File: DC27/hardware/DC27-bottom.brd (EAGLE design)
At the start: 102.4 x 117.6 mm, 97 parts, among them IC2 LDL112D33R, IC3 FT2232HL-REEL, IC4 93LC46BT-I_OT, J1 PAIRING, J2 JTAG, J3 Battery, J4 Program Port, U2 ESP-WROOM-32, Y1 ABM7-12.000MHZ-D2Y-T

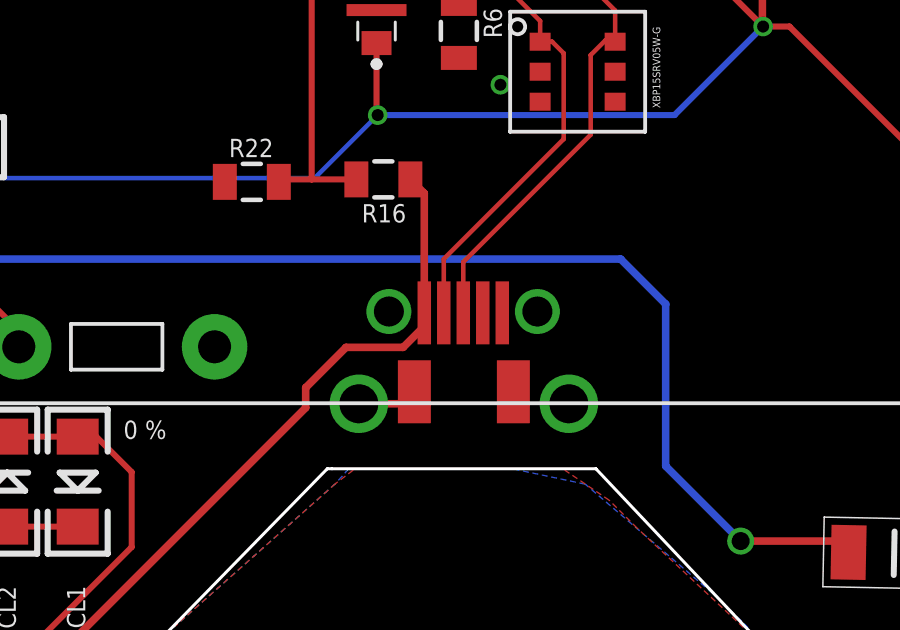
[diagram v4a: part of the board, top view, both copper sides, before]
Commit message: moved usb .15mm closer to edge per first pcb ask
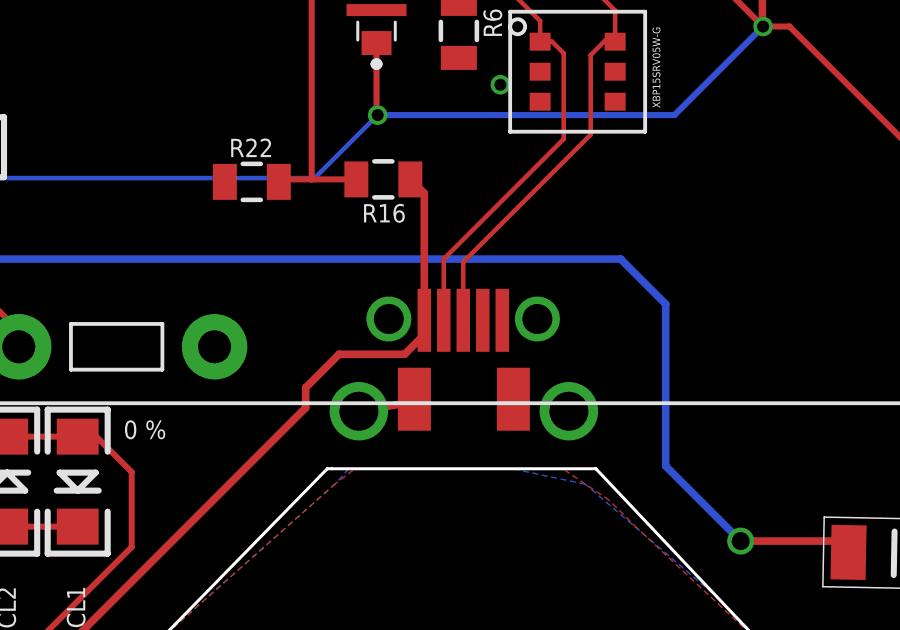
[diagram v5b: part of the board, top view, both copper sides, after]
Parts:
- moved U$3 0.25 mm to (51.2, 27.8)
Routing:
- net VCC5V: track 42.3 -> 43.0 mm
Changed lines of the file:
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@@
 <attribute name="RS_PRICE/STOCK" value="" x="68.550228125" y="45.380659375" size="1.778" layer="27" display="off"/>
 </element>
-<element name="U$3" library="connector" package="DX4R005JJ2" value="DX4R005JJ2DX4R005JJ2" x="51.207428125" y="28.016259375" smashed="yes" rot="R270"/>
+<element name="U$3" library="connector" package="DX4R005JJ2" value="DX4R005JJ2DX4R005JJ2" x="51.207428125" y="27.766259375" smashed="yes" rot="R270"/>
 <element name="RESETTABLE_FUSE" library="passives" package="FUSC3216X55N" value="0ZCJ0050FF2G" x="65.550228125" y="19.282659375" smashed="yes" rot="R358.9">
 <attribute name="3D_PACKAGE" value="" x="47.390459375" y="57.890790625" size="1.778" layer="27" rot="R358.9" display="off"/>
@@
 <via x="37.934228125" y="58.989059375" extent="1-16" drill="0.4"/>
 <via x="48.534228125" y="73.689059375" extent="1-16" drill="0.4"/>
-<wire x1="47.707428125" y1="24.266259375" x2="49.157428125" y2="24.266259375" width="0.254" layer="1"/>
-<wire x1="49.157428125" y1="24.266259375" x2="49.557428125" y2="24.666259375" width="0.254" layer="1"/>
+<wire x1="47.707428125" y1="24.016259375" x2="49.157428125" y2="24.266259375" width="0.254" layer="1"/>
+<wire x1="49.157428125" y1="24.266259375" x2="49.557428125" y2="24.416259375" width="0.254" layer="1"/>
 <via x="40.934228125" y="62.389059375" extent="1-16" drill="0.4"/>
 <via x="54.634228125" y="74.289059375" extent="1-16" drill="0.4"/>
@@
 <wire x1="35.0368625" y1="13.235059375" x2="27.667828125" y2="13.235059375" width="0.254" layer="1"/>
 <wire x1="27.667828125" y1="13.235059375" x2="27.267828125" y2="12.835059375" width="0.254" layer="1"/>
-<wire x1="49.887428125" y1="27.296259375" x2="49.887978125" y2="27.295709375" width="0.254" layer="1"/>
-<wire x1="49.887978125" y1="27.295709375" x2="49.887978125" y2="26.850096875" width="0.254" layer="1"/>
-<wire x1="47.277315625" y1="26.146059375" x2="45.934228125" y2="24.802971875" width="0.254" layer="1"/>
-<wire x1="49.887978125" y1="26.850096875" x2="49.183940625" y2="26.146059375" width="0.254" layer="1"/>
-<wire x1="49.183940625" y1="26.146059375" x2="47.277315625" y2="26.146059375" width="0.254" layer="1"/>
+<wire x1="49.887428125" y1="27.046259375" x2="49.887978125" y2="27.295709375" width="0.254" layer="1"/>
+<wire x1="49.887978125" y1="27.295709375" x2="49.887978125" y2="26.570096875" width="0.254" layer="1"/>
+<wire x1="47.047315625" y1="25.916059375" x2="45.934228125" y2="24.802971875" width="0.254" layer="1"/>
+<wire x1="49.887978125" y1="26.570096875" x2="49.233940625" y2="25.916059375" width="0.254" layer="1"/>
+<wire x1="49.233940625" y1="25.916059375" x2="47.047315625" y2="25.916059375" width="0.254" layer="1"/>
 <wire x1="27.267828125" y1="12.835059375" x2="24.917828125" y2="15.185059375" width="0.254" layer="1"/>
 <wire x1="24.917828125" y1="15.185059375" x2="23.233428125" y2="15.185059375" width="0.254" layer="1"/>
 <wire x1="35.0368625" y1="13.235059375" x2="45.934228125" y2="24.132425" width="0.254" layer="1"/>
 <wire x1="45.934228125" y1="24.132425" x2="45.934228125" y2="24.802971875" width="0.254" layer="1"/>
-<wire x1="49.887428125" y1="27.296259375" x2="49.887428125" y2="31.281459375" width="0.254" layer="1"/>
+<wire x1="49.887428125" y1="27.046259375" x2="49.887428125" y2="31.281459375" width="0.254" layer="1"/>
 <wire x1="49.887428125" y1="31.281459375" x2="49.423428125" y2="31.745459375" width="0.254" layer="1"/>
 <wire x1="23.233428125" y1="15.185059375" x2="23.233428125" y2="15.970759375" width="0.254" layer="1"/>
@@
 <contactref element="IC3" pad="8"/>
 <contactref element="U$2" pad="P6"/>
-<wire x1="51.187428125" y1="27.296259375" x2="51.187428125" y2="28.989059375" width="0.1524" layer="1"/>
+<wire x1="51.187428125" y1="27.046259375" x2="51.187428125" y2="28.989059375" width="0.1524" layer="1"/>
 <wire x1="52.334228125" y1="39.489059375" x2="53.584228125" y2="38.239059375" width="0.1524" layer="1"/>
 <wire x1="52.334228125" y1="39.489059375" x2="52.334228125" y2="56.847859375" width="0.1524" layer="1"/>
@@
 <wire x1="53.749828125" y1="36.334259375" x2="54.149828125" y2="36.334259375" width="0.1524" layer="1"/>
 <wire x1="54.534228125" y1="33.089059375" x2="54.534228125" y2="35.949859375" width="0.1524" layer="1"/>
-<wire x1="50.537428125" y1="27.296259375" x2="50.537428125" y2="29.092259375" width="0.1524" layer="1"/>
+<wire x1="50.537428125" y1="27.046259375" x2="50.537428125" y2="29.092259375" width="0.1524" layer="1"/>
 <wire x1="50.537428125" y1="29.092259375" x2="54.534228125" y2="33.089059375" width="0.1524" layer="1"/>
 </signal>

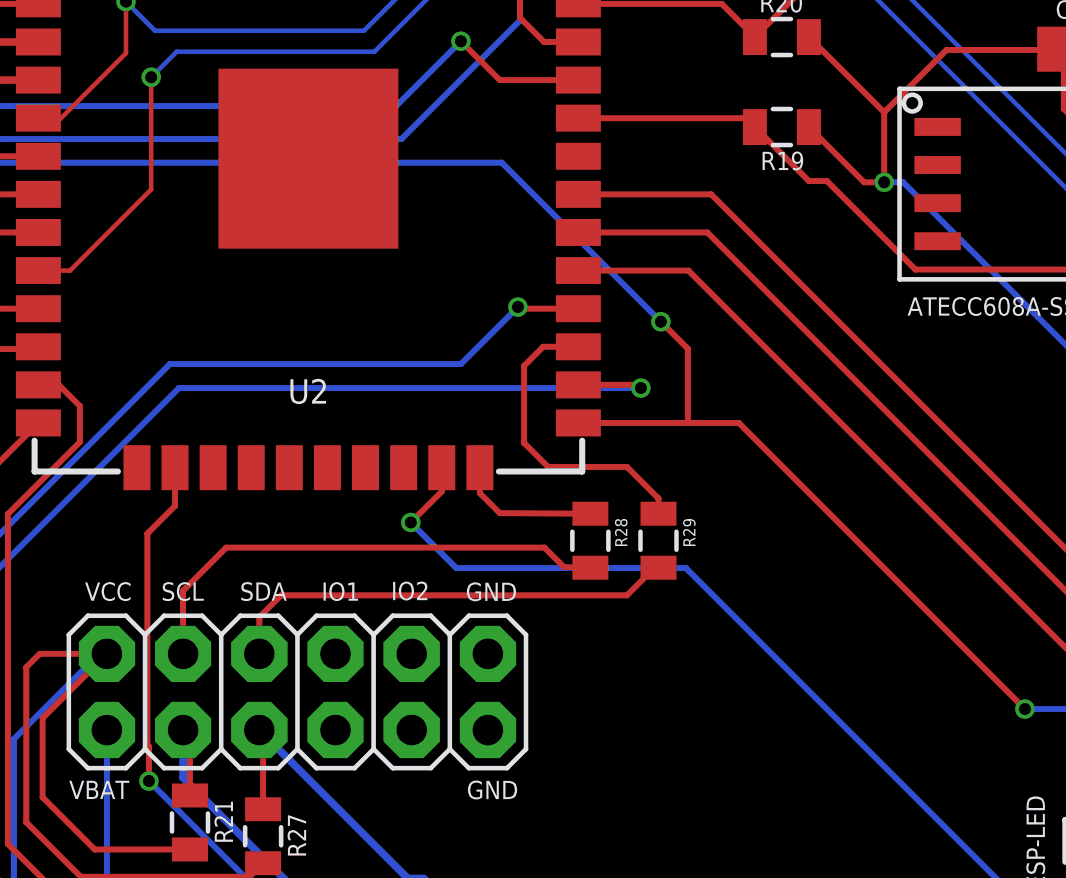
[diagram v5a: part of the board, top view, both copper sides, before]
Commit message: fixed i2c pull ups to be actual pull ups
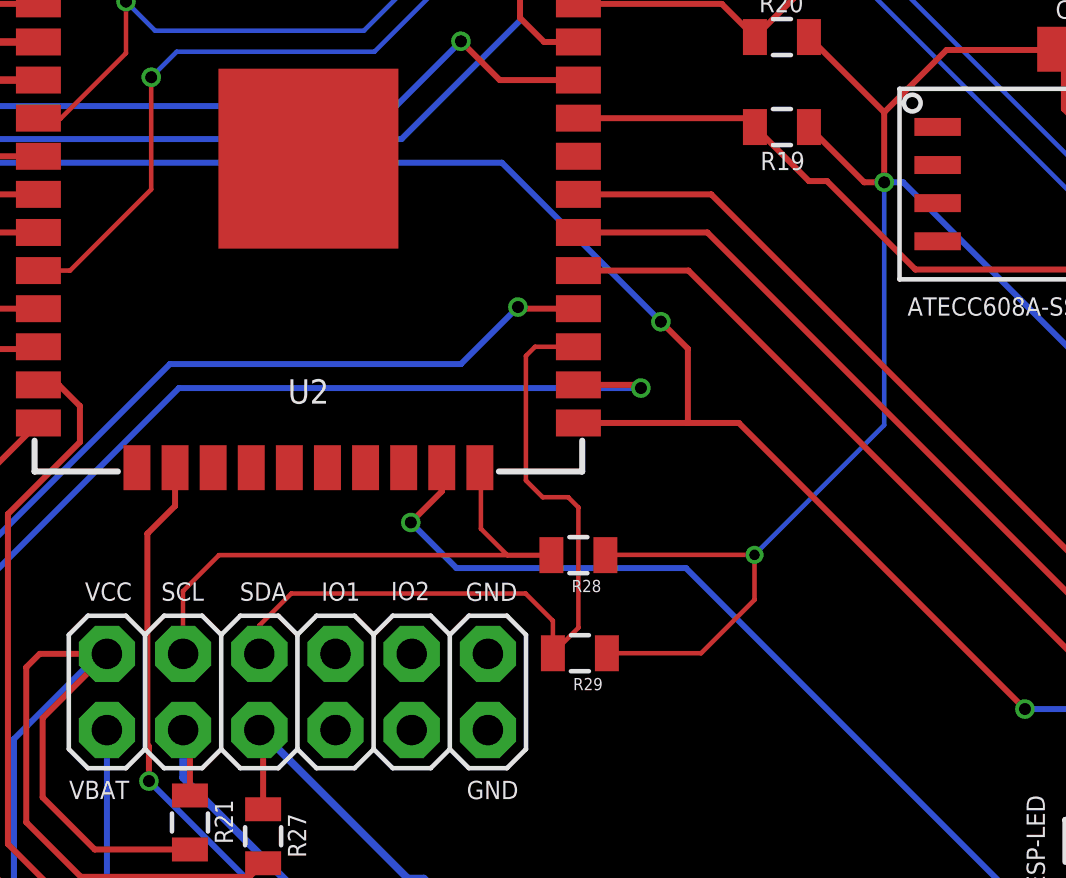
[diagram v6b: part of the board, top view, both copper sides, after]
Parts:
- moved R29 4.57 mm to (60.3, 88.8), turned to 180 degrees
- moved R28 0.62 mm to (60.2, 92.1), turned to 180 degrees
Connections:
- removed net N$1: R28.2, TOP-BOT-CONNECTOR.4
- removed net N$2: R29.2, TOP-BOT-CONNECTOR.6
- net SCL-2: now also R28.2, TOP-BOT-CONNECTOR.4; no longer R28.1
- net SDA-2: now also R29.2, TOP-BOT-CONNECTOR.6; no longer R29.1
- net VCC: now also R28.1, R29.1
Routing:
- net VCC: track 641.5 -> 667.9 mm, vias 11 -> 12
- net N$1: track 16.5 -> 0.00 mm
- net SDA-2: track 10.4 -> 26.0 mm
- net N$2: track 15.2 -> 0.00 mm
- net SCL-2: track 4.81 -> 19.6 mm
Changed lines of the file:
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@@
 <element name="U$14" library="darknet_parts_library" package="DC27_PUZZLE_ELEMENT_5" value="DC27_PUZZLE_ELEMENT_5" x="52.5" y="29.8" smashed="yes" rot="MR0"/>
 <element name="U$15" library="darknet_parts_library" package="DC27_PUZZLE_ELEMENT_6" value="DC27_PUZZLE_ELEMENT_6" x="50.9420875" y="38.833484375" smashed="yes" rot="MR0"/>
-<element name="R28" library="dc-26" package="0805" value="2.2 K" x="60.65" y="92.6" smashed="yes" rot="R270">
-<attribute name="NAME" x="61.4755" y="93.362" size="0.4064" layer="25" rot="R270"/>
-<attribute name="VALUE" x="59.253" y="93.616" size="0.4064" layer="27" rot="R270"/>
+<element name="R28" library="dc-26" package="0805" value="2.2 K" x="60.25" y="92.12" smashed="yes" rot="R180">
+<attribute name="NAME" x="61.012" y="91.2945" size="0.4064" layer="25" rot="R180"/>
+<attribute name="VALUE" x="61.266" y="93.517" size="0.4064" layer="27" rot="R180"/>
 </element>
-<element name="R29" library="dc-26" package="0805" value="2.2 K" x="62.92" y="92.6" smashed="yes" rot="R270">
-<attribute name="NAME" x="63.7455" y="93.362" size="0.4064" layer="25" rot="R270"/>
-<attribute name="VALUE" x="61.523" y="93.616" size="0.4064" layer="27" rot="R270"/>
+<element name="R29" library="dc-26" package="0805" value="2.2 K" x="60.3" y="88.85" smashed="yes" rot="R180">
+<attribute name="NAME" x="61.062" y="88.0245" size="0.4064" layer="25" rot="R180"/>
+<attribute name="VALUE" x="61.316" y="90.247" size="0.4064" layer="27" rot="R180"/>
 </element>
 </elements>
@@
 <wire x1="70.442975" y1="106.8803125" x2="72.520921875" y2="108.958259375" width="0.2" layer="1"/>
 <wire x1="72.520921875" y1="108.958259375" x2="76.166228125" y2="108.958259375" width="0.2" layer="1"/>
+<contactref element="R28" pad="1"/>
+<contactref element="R29" pad="1"/>
+<wire x1="70.442975" y1="104.54813125" x2="70.442975" y2="96.452975" width="0.1524" layer="16"/>
+<wire x1="70.442975" y1="96.452975" x2="66.12" y2="92.13" width="0.1524" layer="16"/>
+<via x="66.12" y="92.13" extent="1-16" drill="0.35"/>
+<wire x1="66.12" y1="92.13" x2="61.16" y2="92.13" width="0.1524" layer="1"/>
+<wire x1="61.16" y1="92.13" x2="61.15" y2="92.12" width="0.1524" layer="1"/>
+<wire x1="61.2" y1="88.85" x2="64.34" y2="88.85" width="0.1524" layer="1"/>
+<wire x1="66.12" y1="90.63" x2="66.12" y2="92.13" width="0.1524" layer="1"/>
+<wire x1="64.34" y1="88.85" x2="66.12" y2="90.63" width="0.1524" layer="1"/>
 </signal>
 <signal name="VBAT" class="2">
@@
 <signal name="SCL-2">
 <contactref element="U2" pad="24"/>
-<contactref element="R28" pad="1"/>
-<wire x1="56.965228125" y1="95.035059375" x2="56.965228125" y2="94.184771875" width="0.2" layer="1"/>
-<wire x1="57.63" y1="93.52" x2="60.65" y2="93.5" width="0.2" layer="1"/>
-<wire x1="56.965228125" y1="94.184771875" x2="57.63" y2="93.52" width="0.2" layer="1"/>
+<contactref element="TOP-BOT-CONNECTOR" pad="4"/>
+<contactref element="R28" pad="2"/>
+<wire x1="56.965228125" y1="95.035059375" x2="57" y2="95.0002875" width="0.1524" layer="1"/>
+<wire x1="57" y1="95.0002875" x2="57" y2="93" width="0.1524" layer="1"/>
+<wire x1="57" y1="93" x2="57.88" y2="92.12" width="0.1524" layer="1"/>
+<wire x1="57.88" y1="92.12" x2="59.35" y2="92.12" width="0.1524" layer="1"/>
+<wire x1="59.35" y1="92.12" x2="48.27" y2="92.12" width="0.1524" layer="1"/>
+<wire x1="48.27" y1="92.12" x2="47.07" y2="90.92" width="0.1524" layer="1"/>
+<wire x1="47.07" y1="90.92" x2="47.07" y2="88.8332875" width="0.1524" layer="1"/>
+<wire x1="47.07" y1="88.8332875" x2="47.074228125" y2="88.829059375" width="0.1524" layer="1"/>
 </signal>
 <signal name="SDA-2">
 <contactref element="U2" pad="27"/>
-<contactref element="R29" pad="1"/>
-<wire x1="60.250228125" y1="99.065059375" x2="59.075059375" y2="99.065059375" width="0.2" layer="1"/>
-<wire x1="58.44" y1="98.43" x2="58.44" y2="95.86" width="0.2" layer="1"/>
-<wire x1="58.44" y1="95.86" x2="59.24" y2="95.06" width="0.2" layer="1"/>
-<wire x1="59.24" y1="95.06" x2="61.87" y2="95.06" width="0.2" layer="1"/>
-<wire x1="61.87" y1="95.06" x2="62.92" y2="94.01" width="0.2" layer="1"/>
-<wire x1="62.92" y1="94.01" x2="62.92" y2="93.5" width="0.2" layer="1"/>
-<wire x1="59.075059375" y1="99.065059375" x2="58.44" y2="98.43" width="0.2" layer="1"/>
-</signal>
-<signal name="N$1">
-<contactref element="TOP-BOT-CONNECTOR" pad="4"/>
-<contactref element="R28" pad="2"/>
-<wire x1="60.65" y1="91.7" x2="59.77" y2="91.72" width="0.2" layer="1"/>
-<wire x1="59.77" y1="91.72" x2="59.12" y2="92.37" width="0.2" layer="1"/>
-<wire x1="59.12" y1="92.37" x2="48.51" y2="92.37" width="0.2" layer="1"/>
-<wire x1="48.51" y1="92.37" x2="47.07" y2="90.93" width="0.2" layer="1"/>
-<wire x1="47.07" y1="90.93" x2="47.07" y2="88.8332875" width="0.2" layer="1"/>
-<wire x1="47.07" y1="88.8332875" x2="47.074228125" y2="88.829059375" width="0.2" layer="1"/>
-</signal>
-<signal name="N$2">
 <contactref element="TOP-BOT-CONNECTOR" pad="6"/>
 <contactref element="R29" pad="2"/>
-<wire x1="62.92" y1="91.7" x2="62.81" y2="91.72" width="0.2" layer="1"/>
-<wire x1="62.81" y1="91.72" x2="61.87" y2="90.78" width="0.2" layer="1"/>
-<wire x1="61.87" y1="90.78" x2="50.4" y2="90.78" width="0.2" layer="1"/>
-<wire x1="50.4" y1="90.78" x2="50.37" y2="90.81" width="0.2" layer="1"/>
-<wire x1="50.37" y1="90.81" x2="49.614228125" y2="90.054228125" width="0.2" layer="1"/>
-<wire x1="49.614228125" y1="90.054228125" x2="49.614228125" y2="88.829059375" width="0.2" layer="1"/>
+<wire x1="59.4" y1="88.85" x2="59.4" y2="89.93" width="0.1524" layer="1"/>
+<wire x1="58.49" y1="90.84" x2="50.68" y2="90.84" width="0.1524" layer="1"/>
+<wire x1="50.68" y1="90.84" x2="49.614228125" y2="89.774228125" width="0.1524" layer="1"/>
+<wire x1="49.614228125" y1="89.774228125" x2="49.614228125" y2="88.829059375" width="0.1524" layer="1"/>
+<wire x1="59.4" y1="89.93" x2="58.49" y2="90.84" width="0.1524" layer="1"/>
+<wire x1="60.250228125" y1="99.065059375" x2="58.805059375" y2="99.065059375" width="0.1524" layer="1"/>
+<wire x1="58.805059375" y1="99.065059375" x2="58.5" y2="98.76" width="0.1524" layer="1"/>
+<wire x1="58.5" y1="98.76" x2="58.5" y2="94.61" width="0.1524" layer="1"/>
+<wire x1="59.06" y1="94.05" x2="59.91" y2="94.05" width="0.1524" layer="1"/>
+<wire x1="59.91" y1="94.05" x2="60.25" y2="93.71" width="0.1524" layer="1"/>
+<wire x1="60.25" y1="89.7" x2="59.4" y2="88.85" width="0.1524" layer="1"/>
+<wire x1="58.5" y1="94.61" x2="59.06" y2="94.05" width="0.1524" layer="1"/>
+<wire x1="60.25" y1="93.71" x2="60.25" y2="89.7" width="0.1524" layer="1"/>
 </signal>
 </signals>
